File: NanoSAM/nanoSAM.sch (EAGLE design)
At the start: 85 parts, among them J1 POWER_JACK, U1 LTC3260EMSEPBF

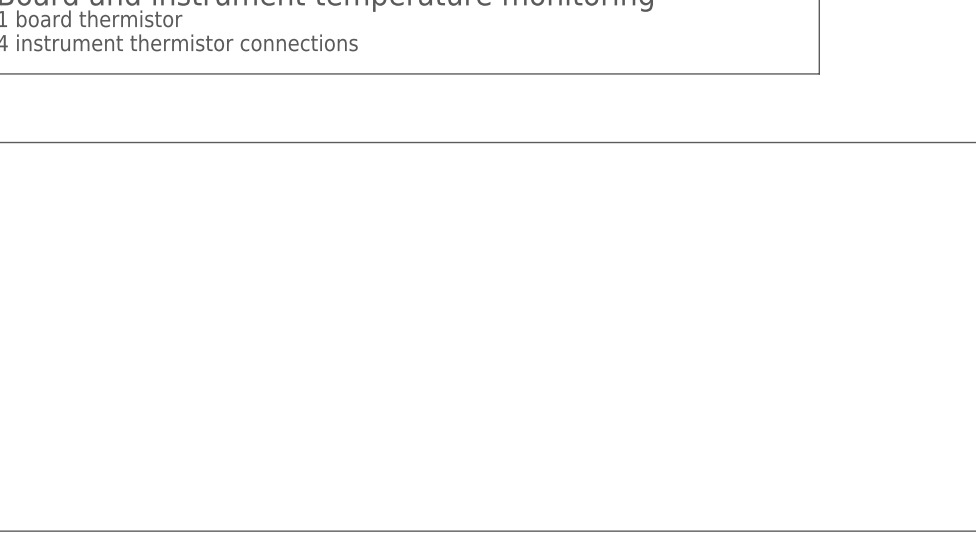
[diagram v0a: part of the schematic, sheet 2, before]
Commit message: Added Coin Cell Battery library, schematic, and board.
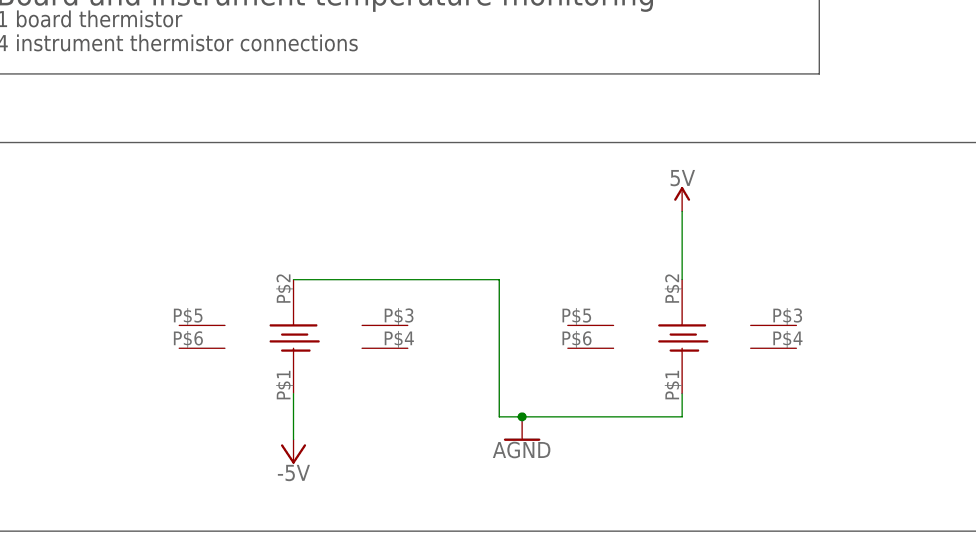
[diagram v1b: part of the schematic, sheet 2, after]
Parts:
- added U$20, U$21: CR2032, BatteryCR2032:CR2032
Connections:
- net -5V: now also U$20.P$2
- net 5V: now also U$21.P$1
- net AGND: now also U$20.P$1, U$21.P$2
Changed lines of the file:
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@@
 <part name="SUPPLY30" library="supply2" library_urn="urn:adsk.eagle:library:372" deviceset="DGND" device=""/>
 <part name="SUPPLY32" library="supply2" library_urn="urn:adsk.eagle:library:372" deviceset="DGND" device=""/>
+<part name="U$20" library="BatteryCR2032" deviceset="CR2032" device=""/>
+<part name="U$21" library="BatteryCR2032" deviceset="CR2032" device=""/>
+<part name="U$22" library="SparkFun-PowerSymbols" library_urn="urn:adsk.eagle:library:530" deviceset="AGND" device=""/>
+<part name="SUPPLY22" library="supply1" library_urn="urn:adsk.eagle:library:371" deviceset="-5V" device=""/>
+<part name="SUPPLY27" library="SparkFun-PowerSymbols" library_urn="urn:adsk.eagle:library:530" deviceset="5V" device=""/>
 </parts>
 <sheets>
@@
 <attribute name="VALUE" x="43.053" y="161.925" size="1.778" layer="96"/>
 </instance>
+<instance part="U$20" gate="G$1" x="48.26" y="38.1" smashed="yes"/>
+<instance part="U$21" gate="G$1" x="91.44" y="38.1" smashed="yes"/>
+<instance part="U$22" gate="G$1" x="73.66" y="20.32" smashed="yes">
+<attribute name="VALUE" x="73.66" y="20.066" size="1.778" layer="96" align="top-center"/>
+</instance>
+<instance part="SUPPLY22" gate="1" x="48.26" y="17.78" smashed="yes">
+<attribute name="VALUE" x="48.26" y="17.526" size="1.778" layer="96" align="top-center"/>
+</instance>
+<instance part="SUPPLY27" gate="G$1" x="91.44" y="45.72" smashed="yes">
+<attribute name="VALUE" x="91.44" y="48.514" size="1.778" layer="96" align="bottom-center"/>
+</instance>
 </instances>
 <busses>
@@
 <pinref part="R26" gate="G$1" pin="2"/>
 </segment>
+<segment>
+<wire x1="91.44" y1="38.1" x2="91.44" y2="45.72" width="0.1524" layer="91"/>
+<pinref part="U$21" gate="G$1" pin="P$1"/>
+<pinref part="SUPPLY27" gate="G$1" pin="5V"/>
+</segment>
 </net>
 <net name="AGND" class="0">
@@
 <pinref part="U$18" gate="G$1" pin="AGND"/>
 <wire x1="236.22" y1="111.76" x2="231.14" y2="111.76" width="0.1524" layer="91"/>
+</segment>
+<segment>
+<pinref part="U$20" gate="G$1" pin="P$1"/>
+<wire x1="48.26" y1="38.1" x2="71.12" y2="38.1" width="0.1524" layer="91"/>
+<wire x1="71.12" y1="38.1" x2="71.12" y2="22.86" width="0.1524" layer="91"/>
+<pinref part="U$21" gate="G$1" pin="P$2"/>
+<wire x1="71.12" y1="22.86" x2="73.66" y2="22.86" width="0.1524" layer="91"/>
+<wire x1="73.66" y1="22.86" x2="91.44" y2="22.86" width="0.1524" layer="91"/>
+<wire x1="91.44" y1="22.86" x2="91.44" y2="25.4" width="0.1524" layer="91"/>
+<pinref part="U$22" gate="G$1" pin="AGND"/>
+<junction x="73.66" y="22.86"/>
 </segment>
 </net>
@@
 <pinref part="R27" gate="G$1" pin="2"/>
 </segment>
-</net>
+<segment>
+<pinref part="U$20" gate="G$1" pin="P$2"/>
+<wire x1="48.26" y1="25.4" x2="48.26" y2="20.32" width="0.1524" layer="91"/>
+<pinref part="SUPPLY22" gate="1" pin="-5V"/>
+</segment>
+</net>

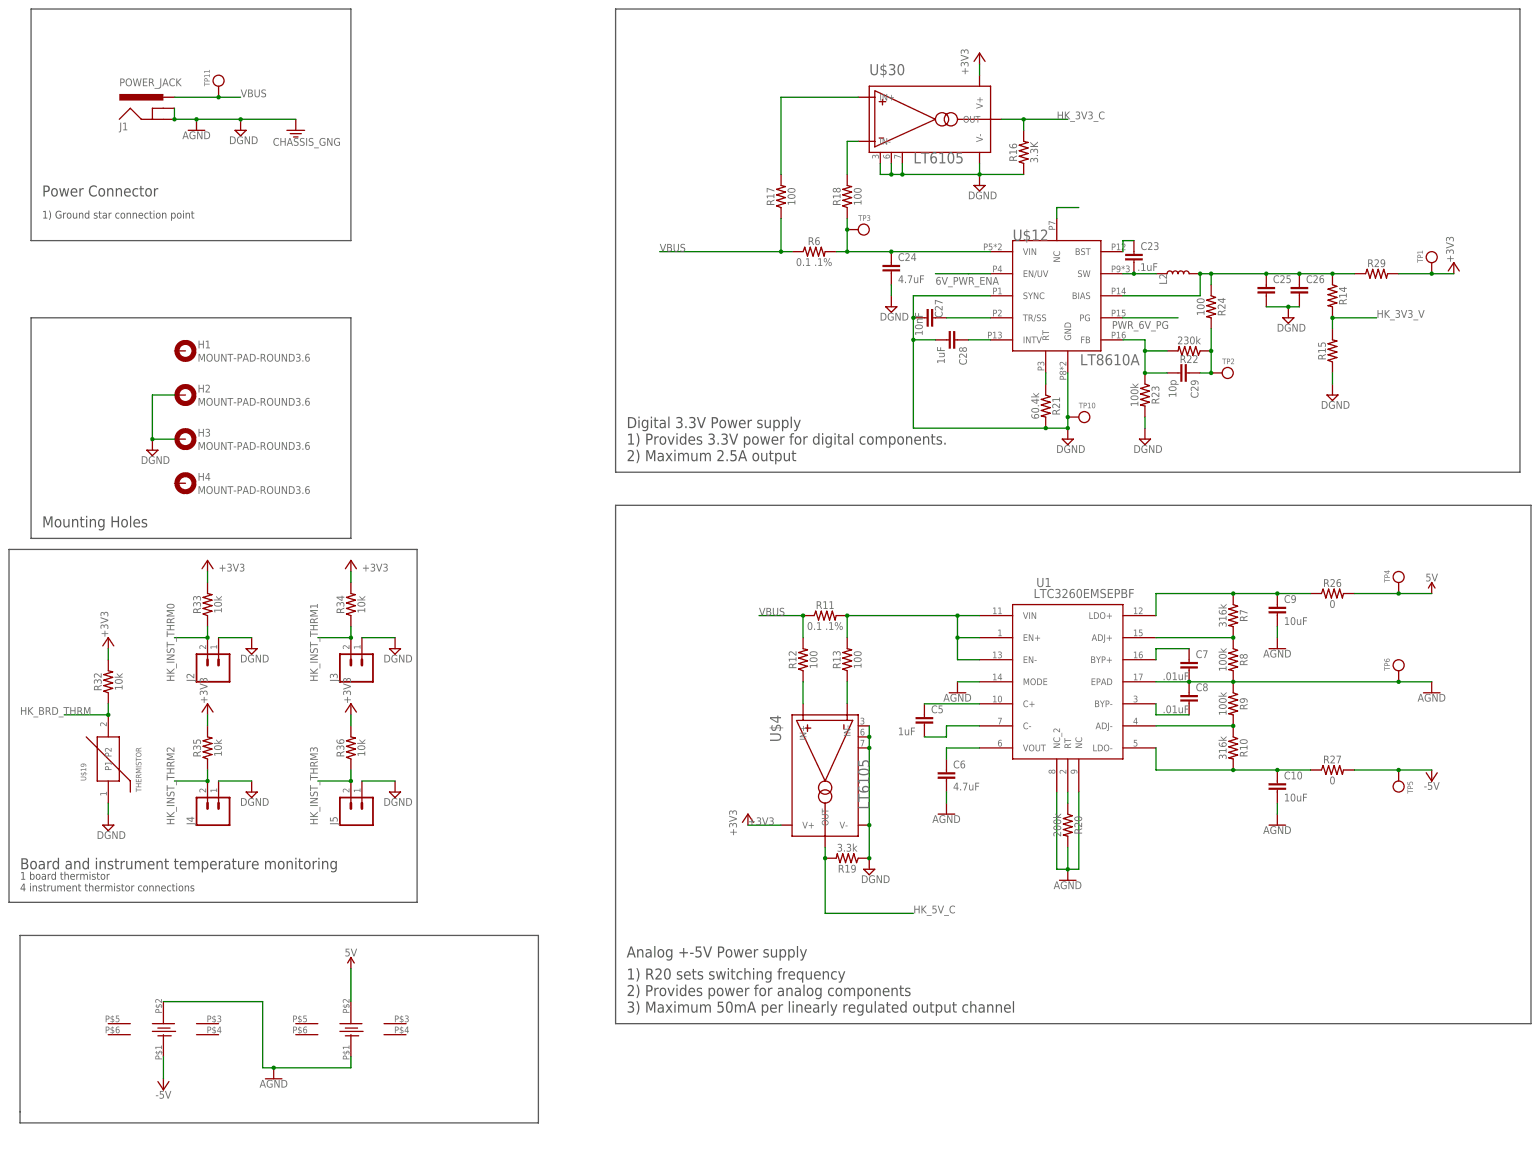
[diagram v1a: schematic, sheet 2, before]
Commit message: added some documentation to schematic, added datasheets folder
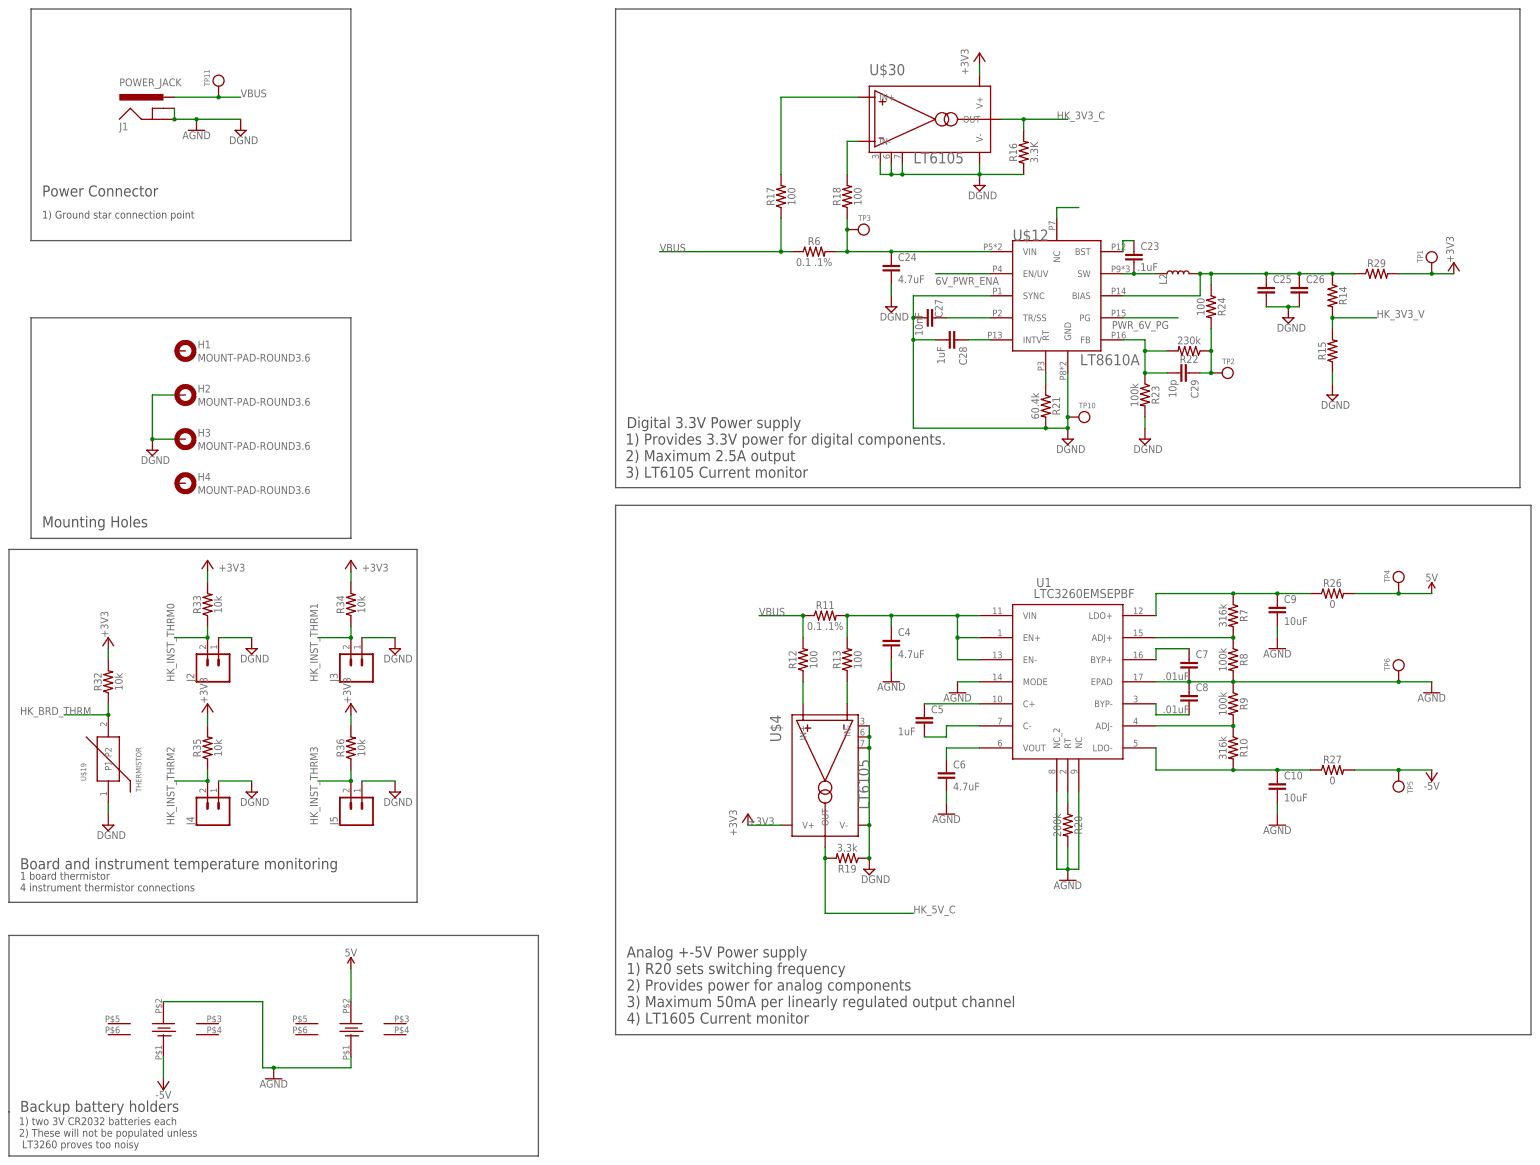
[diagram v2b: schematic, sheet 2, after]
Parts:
- added C4: 4.7uF, SparkFun-Capacitors:4.7UF-1206-16V-(+80/-20%)
- R25: value DNP -> 1M
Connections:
- net AGND: now also C4.2
- net N$15: now also C4.1
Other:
- note added: "1) Provides 3.3V power for digital components. 2) Maximum 2.5A output 3) LT6105 Current monitor"
- note added: "1) R20 sets switching frequency 2) Provides power for analog components 3) Maximum 50mA per linearly regulated output channel 4) LT1605 Current monitor"
- note added: "1) Teensy 4.0 2) SPI bus for ADC and flash 4) Analog inputs used for housekeeping signals"
- note added: "1) two 3V CR2032 batteries each 2) These will not be populated unless LT3260 proves too noisy"
- note added: "Backup battery holders"
- note removed: "1) Provides 3.3V power for digital components. 2) Maximum 2.5A output"
- note removed: "1) R20 sets switching frequency 2) Provides power for analog components 3) Maximum 50mA per linearly regulated output channel"
- note removed: "1) Teensy 4.0 2) Requires 1 SPI bus 3) Requires 1 I2C bus 4) Analog inputs used for housekeeping signals"
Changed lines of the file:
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@@
 <?xml version="1.0" encoding="utf-8"?>
 <!DOCTYPE eagle SYSTEM "eagle.dtd">
-<eagle version="9.5.1">
+<eagle version="9.3.0">
 <drawing>
 <settings>
@@
 <part name="SUPPLY4" library="supply1" library_urn="urn:adsk.eagle:library:371" deviceset="-5V" device=""/>
 <part name="SUPPLY5" library="supply1" library_urn="urn:adsk.eagle:library:371" deviceset="-5V" device=""/>
-<part name="R25" library="SparkFun-Resistors" library_urn="urn:adsk.eagle:library:532" deviceset="RESISTOR" device="0805" package3d_urn="urn:adsk.eagle:package:39651/1" value="DNP"/>
+<part name="R25" library="SparkFun-Resistors" library_urn="urn:adsk.eagle:library:532" deviceset="RESISTOR" device="0805" package3d_urn="urn:adsk.eagle:package:39651/1" value="1M"/>
 <part name="SUPPLY9" library="supply2" library_urn="urn:adsk.eagle:library:372" deviceset="DGND" device=""/>
 <part name="SUPPLY10" library="supply2" library_urn="urn:adsk.eagle:library:372" deviceset="DGND" device=""/>
@@
 <part name="H3" library="holes" library_urn="urn:adsk.eagle:library:237" deviceset="MOUNT-PAD-ROUND" device="3.6" package3d_urn="urn:adsk.eagle:package:14284/1"/>
 <part name="H4" library="holes" library_urn="urn:adsk.eagle:library:237" deviceset="MOUNT-PAD-ROUND" device="3.6" package3d_urn="urn:adsk.eagle:package:14284/1"/>
-<part name="GND2" library="SparkFun-PowerSymbols" library_urn="urn:adsk.eagle:library:530" deviceset="GND2" device="" value="CHASSIS_GNG"/>
 <part name="U$10" library="SparkFun-PowerSymbols" library_urn="urn:adsk.eagle:library:530" deviceset="AGND" device=""/>
 <part name="U$18" library="SparkFun-PowerSymbols" library_urn="urn:adsk.eagle:library:530" deviceset="AGND" device=""/>
@@
 <part name="SUPPLY22" library="supply1" library_urn="urn:adsk.eagle:library:371" deviceset="-5V" device=""/>
 <part name="SUPPLY27" library="SparkFun-PowerSymbols" library_urn="urn:adsk.eagle:library:530" deviceset="5V" device=""/>
+<part name="C4" library="SparkFun-Capacitors" library_urn="urn:adsk.eagle:library:510" deviceset="4.7UF" device="-1206-16V-(+80/-20%)" package3d_urn="urn:adsk.eagle:package:37426/1" value="4.7uF"/>
+<part name="U$23" library="SparkFun-PowerSymbols" library_urn="urn:adsk.eagle:library:530" deviceset="AGND" device=""/>
 </parts>
 <sheets>
@@
 4) Optional R25 feedback resistor - use in place of IC3</text>
 <text x="299.72" y="86.36" size="2.54" layer="97">1) Teensy 4.0
-2) Requires 1 SPI bus
-3) Requires 1 I2C bus
+2) SPI bus for ADC and flash
 4) Analog inputs used for housekeeping signals</text>
 <text x="299.72" y="-17.78" size="2.54" layer="97">1) 128Mbit minimum
@@
 <sheet>
 <plain>
-<wire x1="152.4" y1="266.7" x2="152.4" y2="160.02" width="0.1524" layer="97"/>
-<wire x1="152.4" y1="160.02" x2="360.68" y2="160.02" width="0.1524" layer="97"/>
-<wire x1="360.68" y1="160.02" x2="360.68" y2="266.7" width="0.1524" layer="97"/>
+<wire x1="152.4" y1="266.7" x2="152.4" y2="156.464" width="0.1524" layer="97"/>
+<wire x1="152.4" y1="156.464" x2="360.68" y2="156.464" width="0.1524" layer="97"/>
+<wire x1="360.68" y1="156.464" x2="360.68" y2="266.7" width="0.1524" layer="97"/>
 <wire x1="360.68" y1="266.7" x2="152.4" y2="266.7" width="0.1524" layer="97"/>
 <text x="154.94" y="170.18" size="2.54" layer="97">Digital 3.3V Power supply</text>
-<wire x1="152.4" y1="152.4" x2="152.4" y2="33.02" width="0.1524" layer="97"/>
-<wire x1="152.4" y1="33.02" x2="363.22" y2="33.02" width="0.1524" layer="97"/>
-<wire x1="363.22" y1="33.02" x2="363.22" y2="152.4" width="0.1524" layer="97"/>
+<wire x1="152.4" y1="152.4" x2="152.4" y2="30.48" width="0.1524" layer="97"/>
+<wire x1="152.4" y1="30.48" x2="363.22" y2="30.48" width="0.1524" layer="97"/>
+<wire x1="363.22" y1="30.48" x2="363.22" y2="152.4" width="0.1524" layer="97"/>
 <wire x1="363.22" y1="152.4" x2="152.4" y2="152.4" width="0.1524" layer="97"/>
 <text x="154.94" y="48.26" size="2.54" layer="97">Analog +-5V Power supply</text>
@@
 <wire x1="91.44" y1="195.58" x2="17.78" y2="195.58" width="0.1524" layer="97"/>
 <text x="20.32" y="147.32" size="2.54" layer="97">Mounting Holes</text>
-<text x="154.94" y="35.56" size="2.54" layer="97">1) R20 sets switching frequency
+<text x="154.94" y="33.02" size="2.54" layer="97">1) R20 sets switching frequency
 2) Provides power for analog components
-3) Maximum 50mA per linearly regulated output channel</text>
-<text x="154.94" y="162.56" size="2.54" layer="97">1) Provides 3.3V power for digital components.
-2) Maximum 2.5A output</text>
+3) Maximum 50mA per linearly regulated output channel
+4) LT1605 Current monitor</text>
+<text x="154.686" y="158.75" size="2.54" layer="97">1) Provides 3.3V power for digital components.
+2) Maximum 2.5A output
+3) LT6105 Current monitor</text>
 <wire x1="12.7" y1="60.96" x2="12.7" y2="142.24" width="0.1524" layer="97"/>
 <wire x1="12.7" y1="142.24" x2="106.68" y2="142.24" width="0.1524" layer="97"/>
@@
 <text x="15.24" y="63.5" size="1.778" layer="97">1 board thermistor
 4 instrument thermistor connections</text>
-<wire x1="15.24" y1="12.7" x2="15.24" y2="10.16" width="0.1524" layer="97"/>
-<wire x1="15.24" y1="10.16" x2="134.62" y2="10.16" width="0.1524" layer="97"/>
-<wire x1="134.62" y1="10.16" x2="134.62" y2="53.34" width="0.1524" layer="97"/>
-<wire x1="134.62" y1="53.34" x2="15.24" y2="53.34" width="0.1524" layer="97"/>
-<wire x1="15.24" y1="53.34" x2="15.24" y2="12.7" width="0.1524" layer="97"/>
+<wire x1="12.7" y1="12.7" x2="12.7" y2="2.54" width="0.1524" layer="97"/>
+<wire x1="12.7" y1="2.54" x2="134.62" y2="2.54" width="0.1524" layer="97"/>
+<wire x1="134.62" y1="2.54" x2="134.62" y2="53.34" width="0.1524" layer="97"/>
+<wire x1="134.62" y1="53.34" x2="12.7" y2="53.34" width="0.1524" layer="97"/>
+<wire x1="12.7" y1="53.34" x2="12.7" y2="12.7" width="0.1524" layer="97"/>
+<text x="15.24" y="12.7" size="2.54" layer="97">Backup battery holders</text>
+<text x="14.986" y="4.318" size="1.778" layer="97">1) two 3V CR2032 batteries each
+2) These will not be populated unless
+ LT3260 proves too noisy</text>
 </plain>
 <instances>
@@
 <attribute name="VALUE" x="56.134" y="155.0162" size="1.778" layer="96"/>
 </instance>
-<instance part="GND2" gate="G$1" x="78.74" y="238.76" smashed="yes">
-<attribute name="VALUE" x="81.28" y="236.982" size="1.778" layer="96" align="top-center"/>
-</instance>
 <instance part="U$10" gate="G$1" x="228.6" y="81.28" smashed="yes">
 <attribute name="VALUE" x="228.6" y="81.026" size="1.778" layer="96" align="top-center"/>
@@
 <instance part="SUPPLY27" gate="G$1" x="91.44" y="45.72" smashed="yes">
 <attribute name="VALUE" x="91.44" y="48.514" size="1.778" layer="96" align="bottom-center"/>
+</instance>
+<instance part="C4" gate="G$1" x="215.9" y="119.38" smashed="yes">
+<attribute name="NAME" x="217.424" y="122.301" size="1.778" layer="95" font="vector"/>
+<attribute name="VALUE" x="217.424" y="117.221" size="1.778" layer="96" font="vector"/>
+</instance>
+<instance part="U$23" gate="G$1" x="215.9" y="111.76" smashed="yes">
+<attribute name="VALUE" x="215.9" y="111.506" size="1.778" layer="96" align="top-center"/>
 </instance>
 </instances>
@@
 <pinref part="R11" gate="G$1" pin="2"/>
 <pinref part="U1" gate="A" pin="VIN"/>
-<wire x1="205.74" y1="127" x2="231.14" y2="127" width="0.1524" layer="91"/>
+<wire x1="205.74" y1="127" x2="215.9" y2="127" width="0.1524" layer="91"/>
 <pinref part="U1" gate="A" pin="EN+"/>
+<wire x1="215.9" y1="127" x2="231.14" y2="127" width="0.1524" layer="91"/>
 <wire x1="231.14" y1="127" x2="236.22" y2="127" width="0.1524" layer="91"/>
 <wire x1="231.14" y1="127" x2="231.14" y2="121.92" width="0.1524" layer="91"/>
@@
 <wire x1="205.74" y1="127" x2="205.74" y2="121.92" width="0.1524" layer="91"/>
 <junction x="205.74" y="127"/>
+<pinref part="C4" gate="G$1" pin="1"/>
+<wire x1="215.9" y1="124.46" x2="215.9" y2="127" width="0.1524" layer="91"/>
+<junction x="215.9" y="127"/>
 </segment>
 </net>
@@
 <pinref part="U$22" gate="G$1" pin="AGND"/>
 <junction x="73.66" y="22.86"/>
+</segment>
+<segment>
+<pinref part="C4" gate="G$1" pin="2"/>
+<pinref part="U$23" gate="G$1" pin="AGND"/>
+<wire x1="215.9" y1="116.84" x2="215.9" y2="114.3" width="0.1524" layer="91"/>
 </segment>
 </net>
@@
 <wire x1="55.88" y1="241.3" x2="66.04" y2="241.3" width="0.1524" layer="91"/>
 <junction x="55.88" y="241.3"/>
-<pinref part="GND2" gate="G$1" pin="3.3V"/>
-<wire x1="66.04" y1="241.3" x2="78.74" y2="241.3" width="0.1524" layer="91"/>
-<junction x="66.04" y="241.3"/>
-</segment>
-<segment>
+</segment>
+<segment>

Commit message: added unity gain op-amp buffer for instrument housekeeping
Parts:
- added C16: .1uF, SparkFun-Capacitors:4.7UF-1206-16V-(+80/-20%)
- added U2: LMV324, SparkFun-IC-Amplifiers:LMV324
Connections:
- net +3V3: now also C16.1, U2G5.P$V+
- net DGND: now also C16.2, U2G1.-IN, U2G2.-IN, U2G3.-IN, U2G4.-IN, U2G5.P$V-
- net HK_INST_THRM0: now also U2G1.+IN, U2G1.OUT
- net HK_INST_THRM1: now also U2G2.+IN, U2G2.OUT
- net HK_INST_THRM2: now also U2G3.+IN, U2G3.OUT
- net HK_INST_THRM3: now also U2G4.+IN, U2G4.OUT
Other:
- moved on the sheet: C10, C23, C24, C25, C26, C27, C28, C29, C4, C5, C6, C7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
